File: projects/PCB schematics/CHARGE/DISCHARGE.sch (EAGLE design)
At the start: 0 parts

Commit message: RTDS - Rev A.
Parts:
- added J1, J2: 770966-1, IowaFormula:770966-1
- added R1, R2, R3, R4, R5, R6: 560, PF1262:PF1262-HEATSINKTO126
- added U$1: PNC113, IowaFormula:PNC113
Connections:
- new net DISCHARGE_COIL+: U$1.X1
- new net DISCHARGE_COIL-: U$1.X2
- new net HEATSINK: R1G$1.1, R2G$1.1, R3G$1.1, R4G$1.1, R5G$1.1, R6G$1.1
- new net HV-: J2.1, J2.2, R6G$2.1
- new net MOTORCONTROLLER+: J1.1, J1.2, R1G$2.2
- new net N$1: R5G$2.1, R6G$2.2
- new net N$2: R4G$2.1, R5G$2.2
- new net N$3: R3G$2.1, R4G$2.2
- new net N$4: R2G$2.1, R3G$2.2
- new net N$5: R1G$2.1, R2G$2.2
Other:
- note added: "GLV"
- note added: "NOTE: MOTORCONTROLLER+ and HV- come in from outside of board to PNC. Another wire must be run to HV connectors J1 and J2, where they are then run into board for resistors."
- note added: "TS"

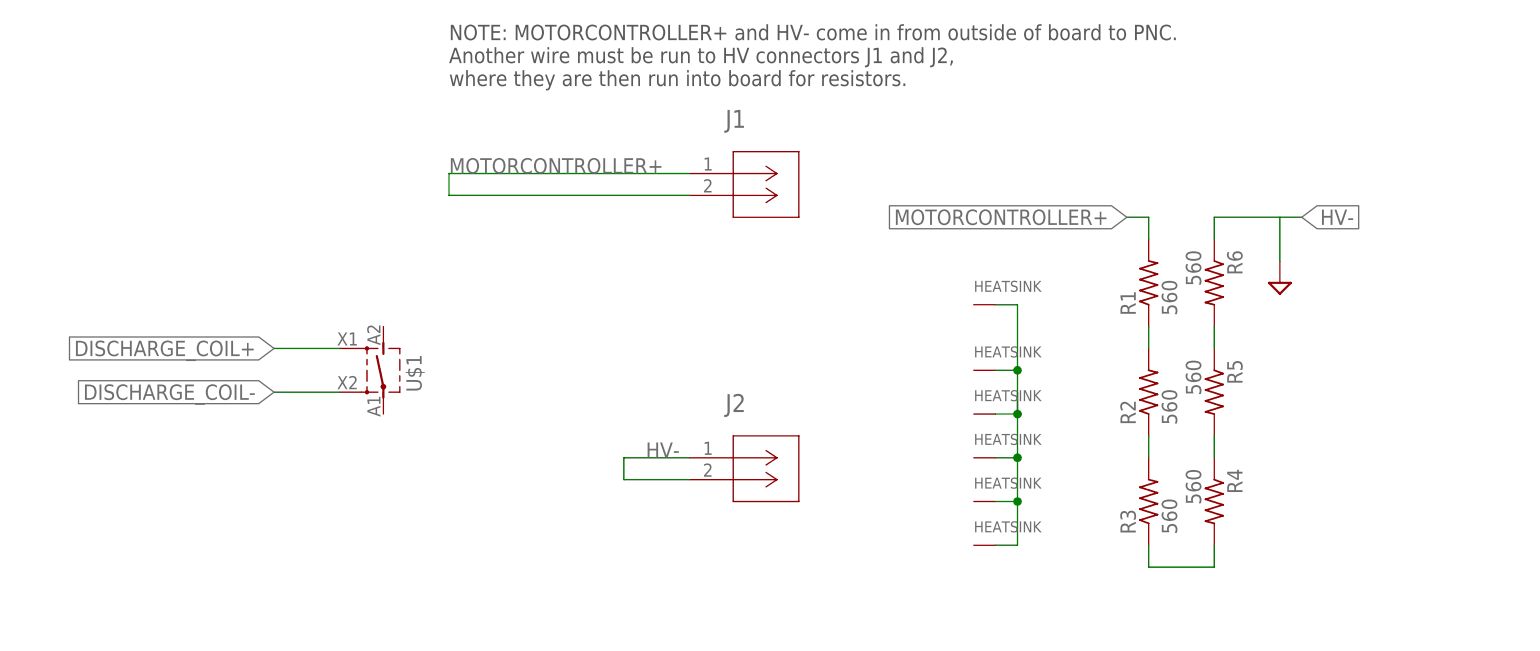
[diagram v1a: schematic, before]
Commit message: POWER - DCDC changes w/ Ryan.
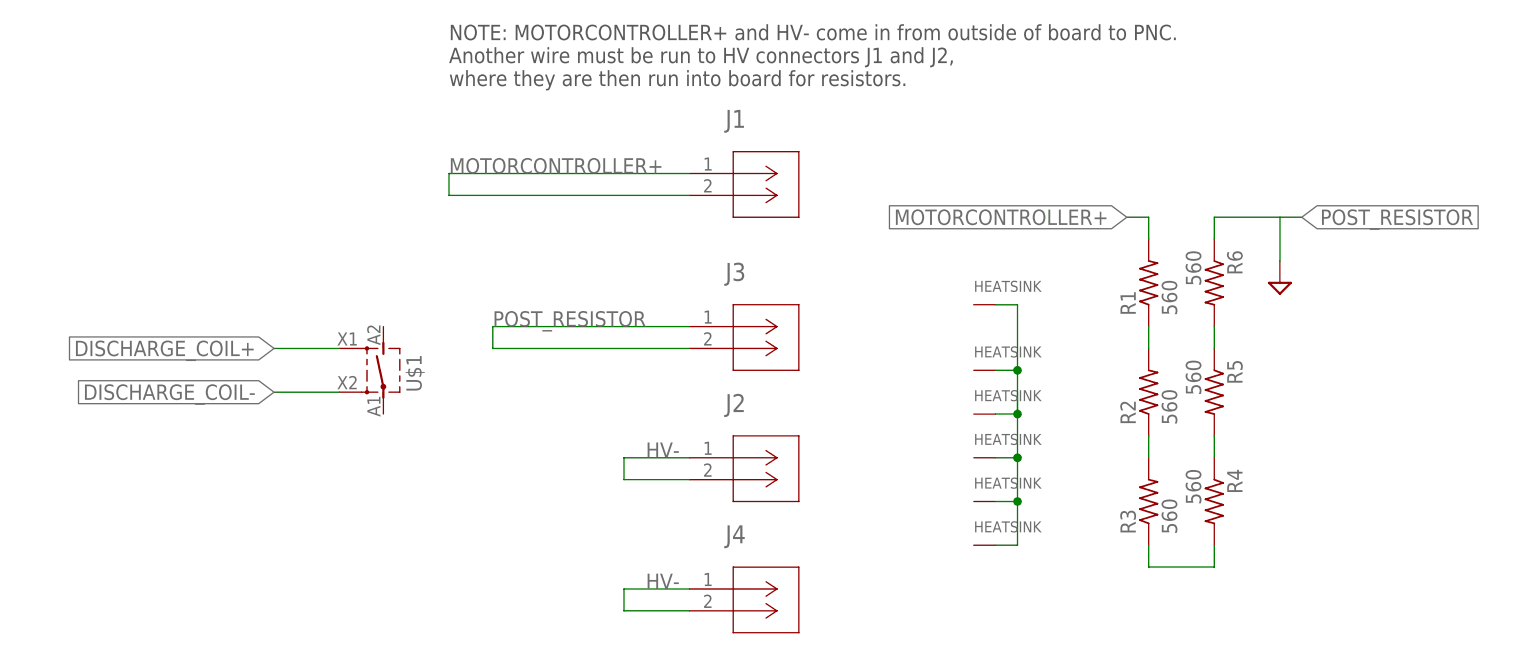
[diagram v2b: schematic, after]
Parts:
- added J3, J4: 770966-1, IowaFormula:770966-1
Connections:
- new net POST_RESISTOR: J3.1, J3.2, R6G$2.1
- net HV-: now also J4.1, J4.2; no longer R6G$2.1
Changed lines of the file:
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@@
 <part name="R6" library="PF1262" deviceset="PF1262-HEATSINK" device="TO126" value="560"/>
 <part name="HV-" library="supply2" library_urn="urn:adsk.eagle:library:372" deviceset="GND1" device=""/>
+<part name="J4" library="IowaFormula" deviceset="770966-1" device=""/>
+<part name="J3" library="IowaFormula" deviceset="770966-1" device=""/>
 </parts>
 <sheets>
@@
 <instance part="R5" gate="G$1" x="116.84" y="17.78" smashed="yes"/>
 <instance part="R6" gate="G$1" x="116.84" y="12.7" smashed="yes"/>
+<instance part="J4" gate="A" x="78.74" y="7.62" smashed="yes">
+<attribute name="NAME" x="82.9056" y="12.9286" size="2.0828" layer="95" ratio="6" rot="SR0"/>
+</instance>
+<instance part="J3" gate="A" x="78.74" y="38.1" smashed="yes">
+<attribute name="NAME" x="82.9056" y="43.4086" size="2.0828" layer="95" ratio="6" rot="SR0"/>
+</instance>
 </instances>
 <busses>
@@
 </segment>
 <segment>
-<pinref part="R6" gate="G$2" pin="1"/>
-<wire x1="139.7" y1="48.26" x2="139.7" y2="50.8" width="0.1524" layer="91"/>
-<wire x1="139.7" y1="50.8" x2="147.32" y2="50.8" width="0.1524" layer="91"/>
-<wire x1="147.32" y1="50.8" x2="147.32" y2="45.72" width="0.1524" layer="91"/>
-<pinref part="HV-" gate="G$1" pin="GND1"/>
-<label x="149.86" y="50.8" size="1.778" layer="95" xref="yes"/>
-<wire x1="147.32" y1="50.8" x2="149.86" y2="50.8" width="0.1524" layer="91"/>
+<pinref part="J4" gate="A" pin="1"/>
+<wire x1="78.74" y1="7.62" x2="71.12" y2="7.62" width="0.1524" layer="91"/>
+<wire x1="71.12" y1="7.62" x2="71.12" y2="5.08" width="0.1524" layer="91"/>
+<pinref part="J4" gate="A" pin="2"/>
+<wire x1="71.12" y1="5.08" x2="78.74" y2="5.08" width="0.1524" layer="91"/>
+<label x="73.66" y="7.62" size="1.778" layer="95"/>
 </segment>
 </net>
@@
 </segment>
 </net>
+<net name="POST_RESISTOR" class="0">
+<segment>
+<pinref part="R6" gate="G$2" pin="1"/>
+<wire x1="139.7" y1="48.26" x2="139.7" y2="50.8" width="0.1524" layer="91"/>
+<wire x1="139.7" y1="50.8" x2="147.32" y2="50.8" width="0.1524" layer="91"/>
+<wire x1="147.32" y1="50.8" x2="147.32" y2="45.72" width="0.1524" layer="91"/>
+<pinref part="HV-" gate="G$1" pin="GND1"/>
+<label x="149.86" y="50.8" size="1.778" layer="95" xref="yes"/>
+<wire x1="147.32" y1="50.8" x2="149.86" y2="50.8" width="0.1524" layer="91"/>
+</segment>
+<segment>
+<pinref part="J3" gate="A" pin="1"/>
+<wire x1="78.74" y1="38.1" x2="55.88" y2="38.1" width="0.1524" layer="91"/>
+<wire x1="55.88" y1="38.1" x2="55.88" y2="35.56" width="0.1524" layer="91"/>
+<pinref part="J3" gate="A" pin="2"/>
+<wire x1="55.88" y1="35.56" x2="78.74" y2="35.56" width="0.1524" layer="91"/>
+<label x="55.88" y="38.1" size="1.778" layer="95"/>
+</segment>
+</net>

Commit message: PROJ - Silkscreen modifications - 50%.
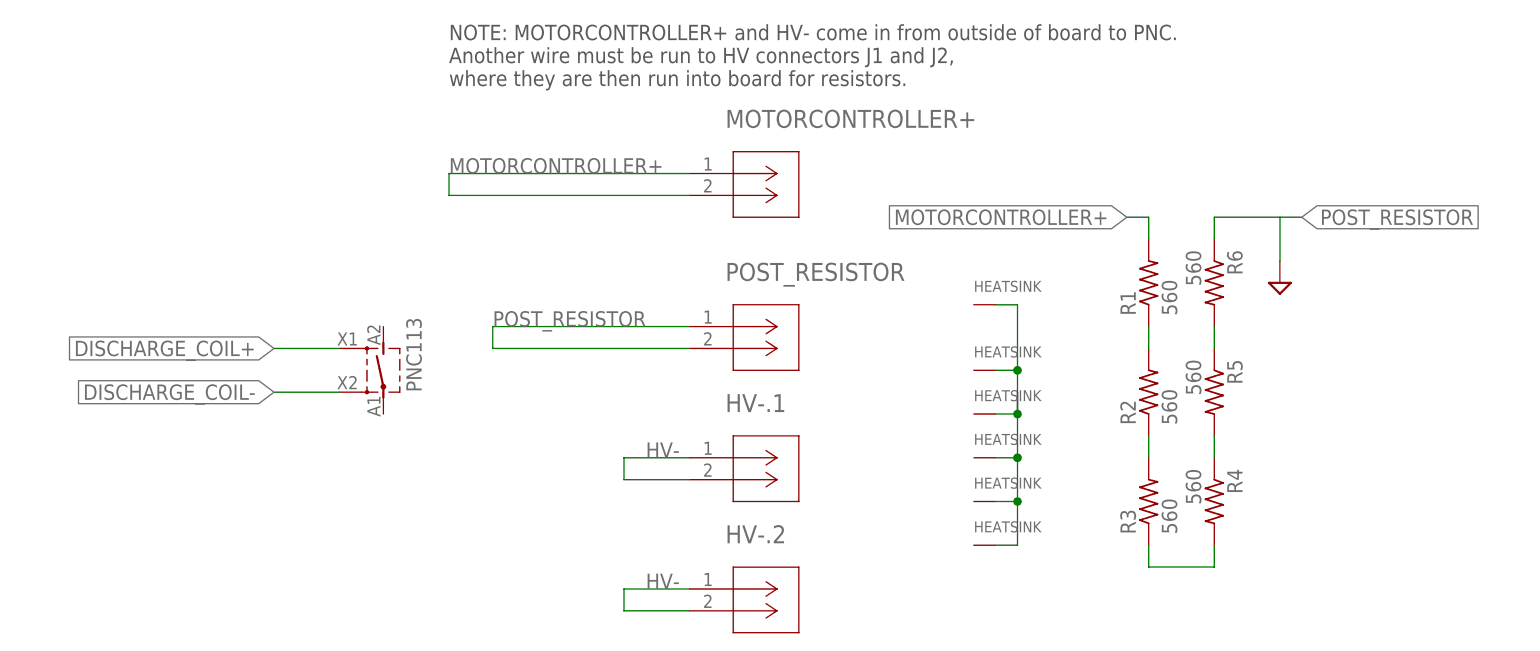
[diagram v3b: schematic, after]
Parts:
- renumbered J1 to MOTORCONTROLLER+, J2 to HV-.1, J3 to POST_RESISTOR, J4 to HV-.2, U$1 to PNC113
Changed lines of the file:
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@@
 </classes>
 <parts>
-<part name="U$1" library="IowaFormula" deviceset="PNC113" device=""/>
-<part name="J1" library="IowaFormula" deviceset="770966-1" device=""/>
-<part name="J2" library="IowaFormula" deviceset="770966-1" device=""/>
+<part name="PNC113" library="IowaFormula" deviceset="PNC113" device=""/>
+<part name="MOTORCONTROLLER+" library="IowaFormula" deviceset="770966-1" device=""/>
+<part name="HV-.1" library="IowaFormula" deviceset="770966-1" device=""/>
 <part name="R1" library="PF1262" deviceset="PF1262-HEATSINK" device="TO126" value="560"/>
 <part name="R2" library="PF1262" deviceset="PF1262-HEATSINK" device="TO126" value="560"/>
@@
 <part name="R6" library="PF1262" deviceset="PF1262-HEATSINK" device="TO126" value="560"/>
 <part name="HV-" library="supply2" library_urn="urn:adsk.eagle:library:372" deviceset="GND1" device=""/>
-<part name="J4" library="IowaFormula" deviceset="770966-1" device=""/>
-<part name="J3" library="IowaFormula" deviceset="770966-1" device=""/>
+<part name="HV-.2" library="IowaFormula" deviceset="770966-1" device=""/>
+<part name="POST_RESISTOR" library="IowaFormula" deviceset="770966-1" device=""/>
 </parts>
 <sheets>
@@
 </plain>
 <instances>
-<instance part="U$1" gate="A" x="43.18" y="33.02" smashed="yes">
+<instance part="PNC113" gate="A" x="43.18" y="33.02" smashed="yes">
 <attribute name="PART" x="47.625" y="30.48" size="1.778" layer="95" rot="R90"/>
 </instance>
-<instance part="J1" gate="A" x="78.74" y="55.88" smashed="yes">
+<instance part="MOTORCONTROLLER+" gate="A" x="78.74" y="55.88" smashed="yes">
 <attribute name="NAME" x="82.9056" y="61.1886" size="2.0828" layer="95" ratio="6" rot="SR0"/>
 </instance>
-<instance part="J2" gate="A" x="78.74" y="22.86" smashed="yes">
+<instance part="HV-.1" gate="A" x="78.74" y="22.86" smashed="yes">
 <attribute name="NAME" x="82.9056" y="28.1686" size="2.0828" layer="95" ratio="6" rot="SR0"/>
 </instance>
@@
 <instance part="R5" gate="G$1" x="116.84" y="17.78" smashed="yes"/>
 <instance part="R6" gate="G$1" x="116.84" y="12.7" smashed="yes"/>
-<instance part="J4" gate="A" x="78.74" y="7.62" smashed="yes">
+<instance part="HV-.2" gate="A" x="78.74" y="7.62" smashed="yes">
 <attribute name="NAME" x="82.9056" y="12.9286" size="2.0828" layer="95" ratio="6" rot="SR0"/>
 </instance>
-<instance part="J3" gate="A" x="78.74" y="38.1" smashed="yes">
+<instance part="POST_RESISTOR" gate="A" x="78.74" y="38.1" smashed="yes">
 <attribute name="NAME" x="82.9056" y="43.4086" size="2.0828" layer="95" ratio="6" rot="SR0"/>
 </instance>
@@
 <net name="MOTORCONTROLLER+" class="0">
 <segment>
-<pinref part="J1" gate="A" pin="1"/>
+<pinref part="MOTORCONTROLLER+" gate="A" pin="1"/>
 <wire x1="78.74" y1="55.88" x2="50.8" y2="55.88" width="0.1524" layer="91"/>
 <wire x1="50.8" y1="55.88" x2="50.8" y2="53.34" width="0.1524" layer="91"/>
-<pinref part="J1" gate="A" pin="2"/>
+<pinref part="MOTORCONTROLLER+" gate="A" pin="2"/>
 <wire x1="50.8" y1="53.34" x2="78.74" y2="53.34" width="0.1524" layer="91"/>
 <label x="50.8" y="55.88" size="1.778" layer="95"/>
@@
 <net name="HV-" class="0">
 <segment>
-<pinref part="J2" gate="A" pin="1"/>
+<pinref part="HV-.1" gate="A" pin="1"/>
 <wire x1="78.74" y1="22.86" x2="71.12" y2="22.86" width="0.1524" layer="91"/>
 <wire x1="71.12" y1="22.86" x2="71.12" y2="20.32" width="0.1524" layer="91"/>
-<pinref part="J2" gate="A" pin="2"/>
+<pinref part="HV-.1" gate="A" pin="2"/>
 <wire x1="71.12" y1="20.32" x2="78.74" y2="20.32" width="0.1524" layer="91"/>
 <label x="73.66" y="22.86" size="1.778" layer="95"/>
 </segment>
 <segment>
-<pinref part="J4" gate="A" pin="1"/>
+<pinref part="HV-.2" gate="A" pin="1"/>
 <wire x1="78.74" y1="7.62" x2="71.12" y2="7.62" width="0.1524" layer="91"/>
 <wire x1="71.12" y1="7.62" x2="71.12" y2="5.08" width="0.1524" layer="91"/>
-<pinref part="J4" gate="A" pin="2"/>
+<pinref part="HV-.2" gate="A" pin="2"/>
 <wire x1="71.12" y1="5.08" x2="78.74" y2="5.08" width="0.1524" layer="91"/>
 <label x="73.66" y="7.62" size="1.778" layer="95"/>
@@
 <wire x1="38.1" y1="35.56" x2="30.48" y2="35.56" width="0.1524" layer="91"/>
 <label x="30.48" y="35.56" size="1.778" layer="95" rot="R180" xref="yes"/>
-<pinref part="U$1" gate="A" pin="X1"/>
+<pinref part="PNC113" gate="A" pin="X1"/>
 </segment>
 </net>
@@
 <wire x1="38.1" y1="30.48" x2="30.48" y2="30.48" width="0.1524" layer="91"/>
 <label x="30.48" y="30.48" size="1.778" layer="95" rot="R180" xref="yes"/>
-<pinref part="U$1" gate="A" pin="X2"/>
+<pinref part="PNC113" gate="A" pin="X2"/>
 </segment>
 </net>
@@
 </segment>
 <segment>
-<pinref part="J3" gate="A" pin="1"/>
+<pinref part="POST_RESISTOR" gate="A" pin="1"/>
 <wire x1="78.74" y1="38.1" x2="55.88" y2="38.1" width="0.1524" layer="91"/>
 <wire x1="55.88" y1="38.1" x2="55.88" y2="35.56" width="0.1524" layer="91"/>
-<pinref part="J3" gate="A" pin="2"/>
+<pinref part="POST_RESISTOR" gate="A" pin="2"/>
 <wire x1="55.88" y1="35.56" x2="78.74" y2="35.56" width="0.1524" layer="91"/>
 <label x="55.88" y="38.1" size="1.778" layer="95"/>

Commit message: PROJ - Final pre-purchase revisions (4 boards still in progress.)
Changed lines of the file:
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@@
 <part name="R5" library="PF1262" deviceset="PF1262-HEATSINK" device="TO126" value="560"/>
 <part name="R6" library="PF1262" deviceset="PF1262-HEATSINK" device="TO126" value="560"/>
-<part name="HV-" library="supply2" library_urn="urn:adsk.eagle:library:372" deviceset="GND1" device=""/>
 <part name="HV-.2" library="IowaFormula" deviceset="770966-1" device=""/>
 <part name="POST_RESISTOR" library="IowaFormula" deviceset="770966-1" device=""/>
@@
 <attribute name="VALUE" x="136.398" y="46.99" size="1.778" layer="96" rot="R270"/>
 </instance>
-<instance part="HV-" gate="G$1" x="147.32" y="43.18" smashed="yes"/>
 <instance part="R1" gate="G$1" x="116.84" y="40.64" smashed="yes"/>
 <instance part="R2" gate="G$1" x="116.84" y="33.02" smashed="yes"/>
@@
 <pinref part="R6" gate="G$2" pin="1"/>
 <wire x1="139.7" y1="48.26" x2="139.7" y2="50.8" width="0.1524" layer="91"/>
-<wire x1="139.7" y1="50.8" x2="147.32" y2="50.8" width="0.1524" layer="91"/>
-<wire x1="147.32" y1="50.8" x2="147.32" y2="45.72" width="0.1524" layer="91"/>
-<pinref part="HV-" gate="G$1" pin="GND1"/>
+<wire x1="139.7" y1="50.8" x2="149.86" y2="50.8" width="0.1524" layer="91"/>
 <label x="149.86" y="50.8" size="1.778" layer="95" xref="yes"/>
-<wire x1="147.32" y1="50.8" x2="149.86" y2="50.8" width="0.1524" layer="91"/>
 </segment>
 <segment>
@@
 which will not be processed correctly with this version.
 </note>
-<note version="8.2" severity="warning">
-Since Version 8.2, EAGLE supports online libraries. The ids
-of those online libraries will not be understood (or retained)
-with this version.
-</note>
 <note version="8.3" severity="warning">
